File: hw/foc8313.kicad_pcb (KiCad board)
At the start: 4 copper layers, 35 x 35 mm, 83 parts, among them J1 Tag Connect, J2 CAN, J3 CAN, J4 Aux, P1 USB_C_Plug, SW1 SW_SPST, U1 DRV8313PWP, U10 XC6206P332MR, U2 STM32F103CBTx, U3 AS5047D, U4 INA240A2D, U5 INA240A2D, U6 ISO1050DUBR, U7 LMR36015SFBRNXR, U8 INA240A2D, U9 ZD24C08AE1-STGMT, X1 X322516MLB4SI

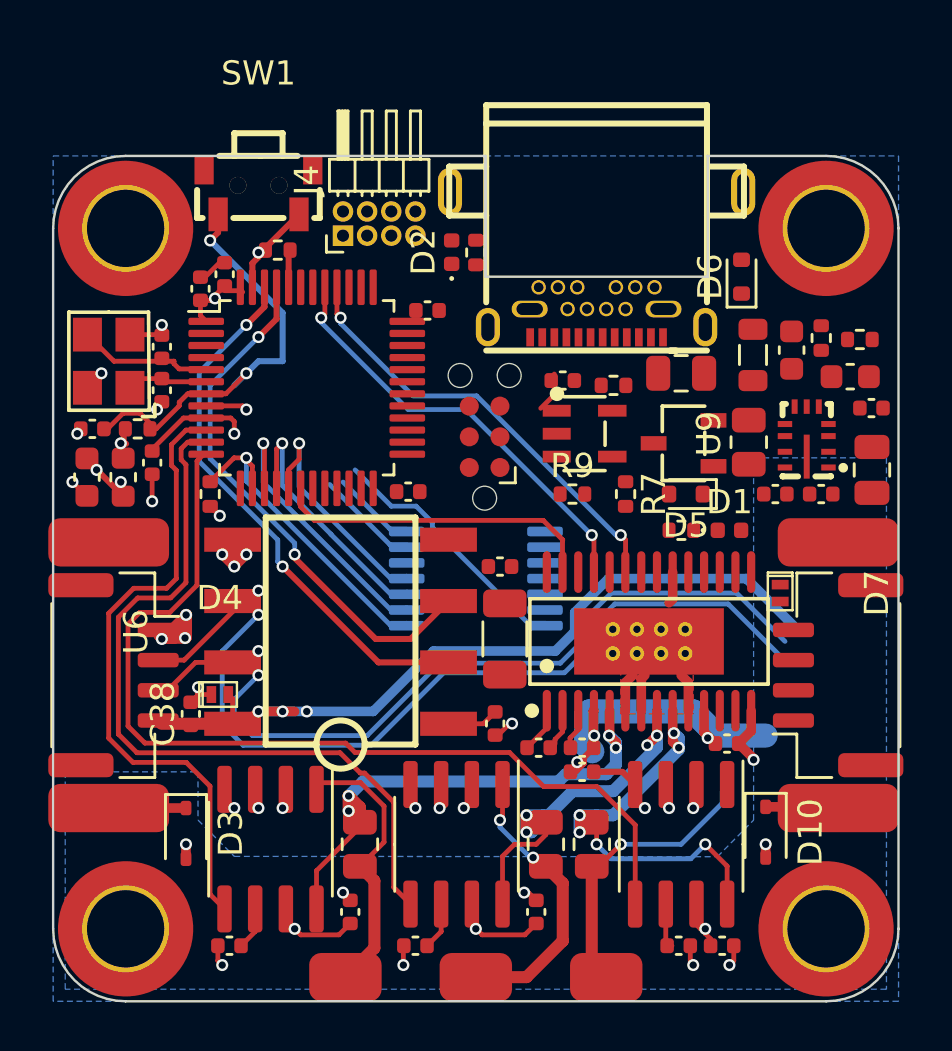
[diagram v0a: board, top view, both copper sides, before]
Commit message: [Hw] Cleaning up 5V section
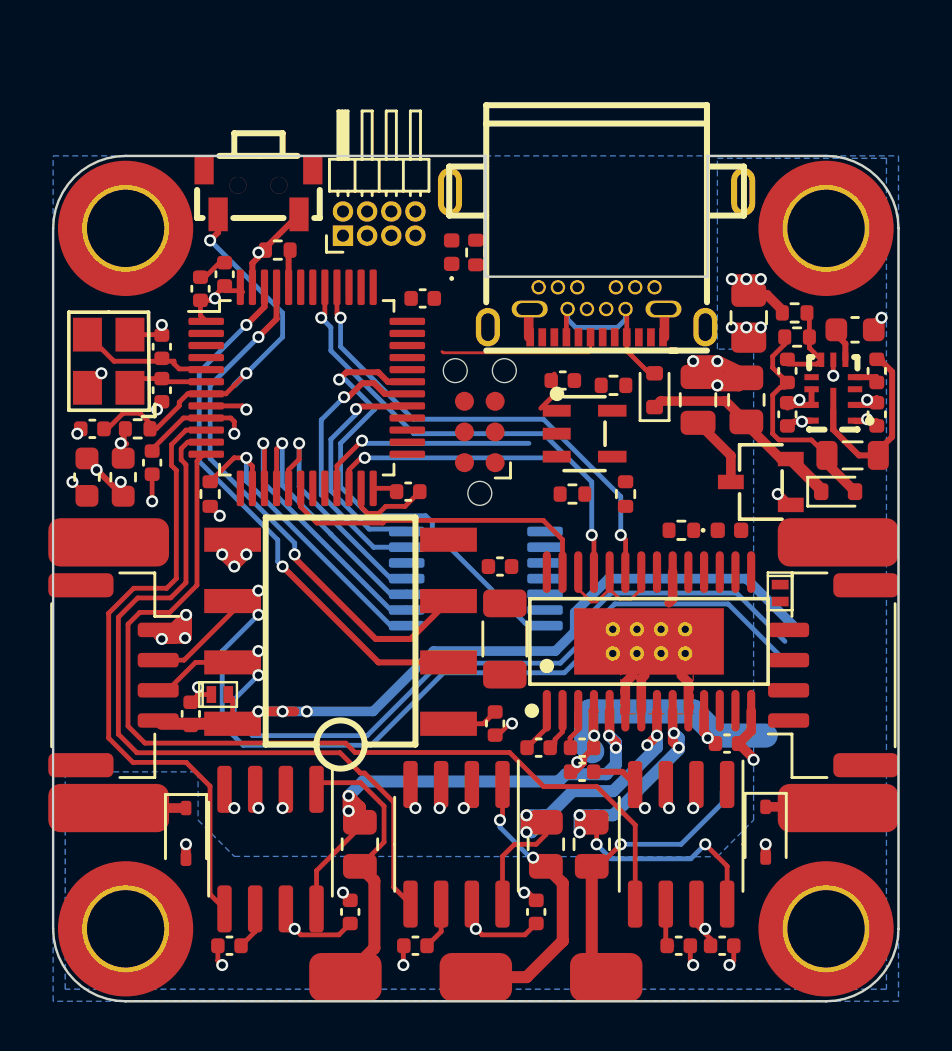
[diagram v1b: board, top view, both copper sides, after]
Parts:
- C18: footprint Capacitor_SMD:C_0603_1608Metric -> Capacitor_SMD:C_0402_1005Metric
- moved C16 8.11 mm to (151.3, 89.2), turned to 90 degrees
- moved D5 6.30 mm to (155.0, 96.4), turned to 0 degrees
- moved D6 5.92 mm to (147.4, 92.2)
- moved L3 5.86 mm to (155.6, 94.9), turned to 0 degrees
- moved C1 4.02 mm to (156.6, 93.2), turned to -90 degrees
- moved U10 3.58 mm to (151.8, 96.0)
- moved C2 3.34 mm to (152.9, 93.2), turned to -90 degrees
- moved R11 2.92 mm to (153.2, 89.0)
- moved U7 2.23 mm to (154.8, 92.2)
- moved C17 1.95 mm to (155.7, 89.7)
- moved C19 1.76 mm to (151.2, 92.6), turned to 90 degrees
- moved C21 1.56 mm to (156.6, 91.4), turned to -90 degrees
- moved C22 1.30 mm to (149.2, 92.6), turned to 90 degrees
- moved R10 1.00 mm to (153.3, 90.0), turned to 0 degrees
- moved C18 0.88 mm to (152.9, 91.4), turned to 90 degrees
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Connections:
- U2 pad 21: unconnected-(U2-PB10-Pad21) -> /I2C.SCL
- U2 pad 22: unconnected-(U2-PB11-Pad22) -> /I2C.SDA
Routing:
- net GND: track 38.7 -> 58.1 mm, vias 27 -> 38
- net Net-(D5-A): track 0.00 -> 9.48 mm
- net /ENC_Z: track 10.6 -> 20.0 mm, vias 0 -> 1
- net /I2C.SCL: track 0.00 -> 9.36 mm, vias 0 -> 1
- net /I2C.SDA: track 0.00 -> 9.02 mm, vias 0 -> 1
- net +5V: track 0.00 -> 8.67 mm
- net Net-(D6-A): track 0.00 -> 8.00 mm
- net Net-(U7-SW): track 0.00 -> 7.77 mm
- net /ENC_B: track 4.22 -> 11.9 mm, vias 0 -> 1
- net /USB_DM: track 0.00 -> 6.76 mm
- net /ENC_A: track 3.45 -> 9.79 mm, vias 0 -> 1
- net /DRV_EN: track 0.00 -> 5.50 mm
- net VCC: track 20.8 -> 25.8 mm, vias 3 -> 8
- net +3.3V: track 13.7 -> 17.7 mm
- net Net-(U7-FB): track 0.00 -> 3.62 mm
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
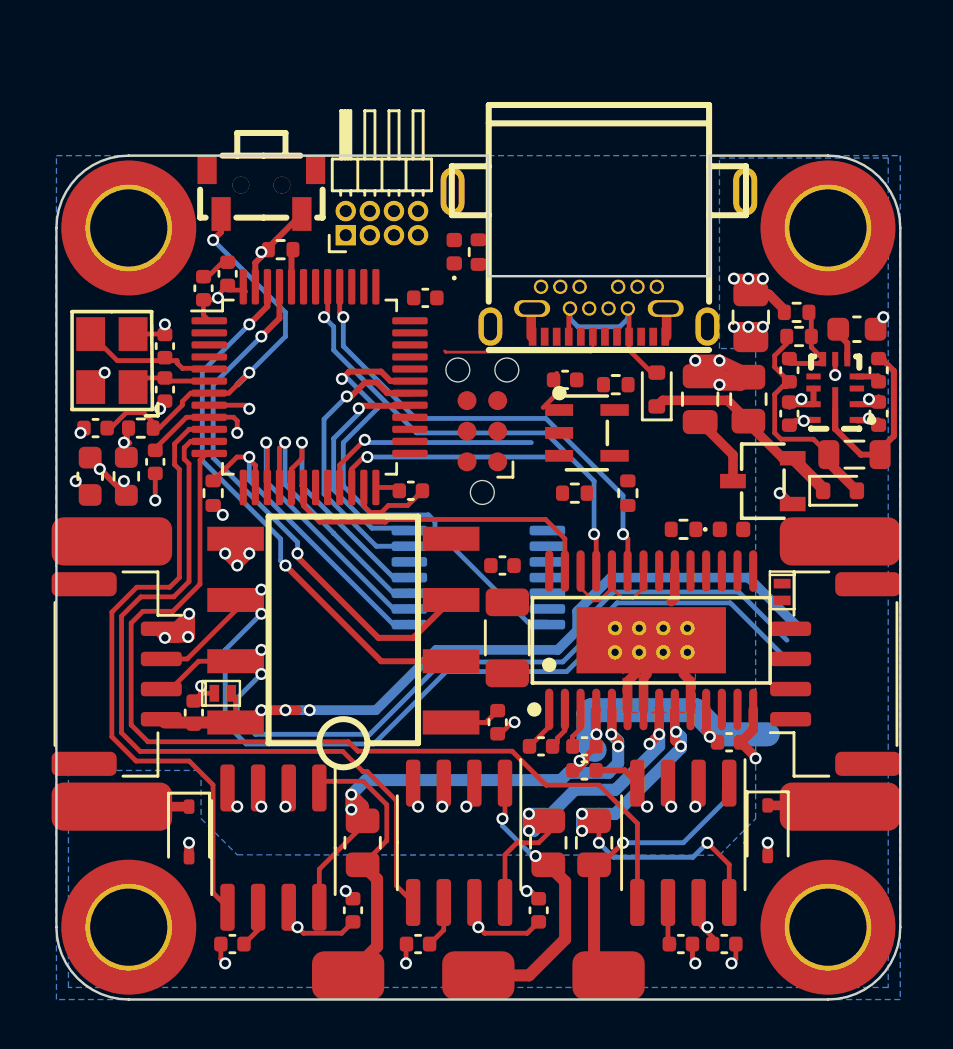
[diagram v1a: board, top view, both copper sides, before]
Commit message: [Hw] User button, tag connect placement, eeprom placement
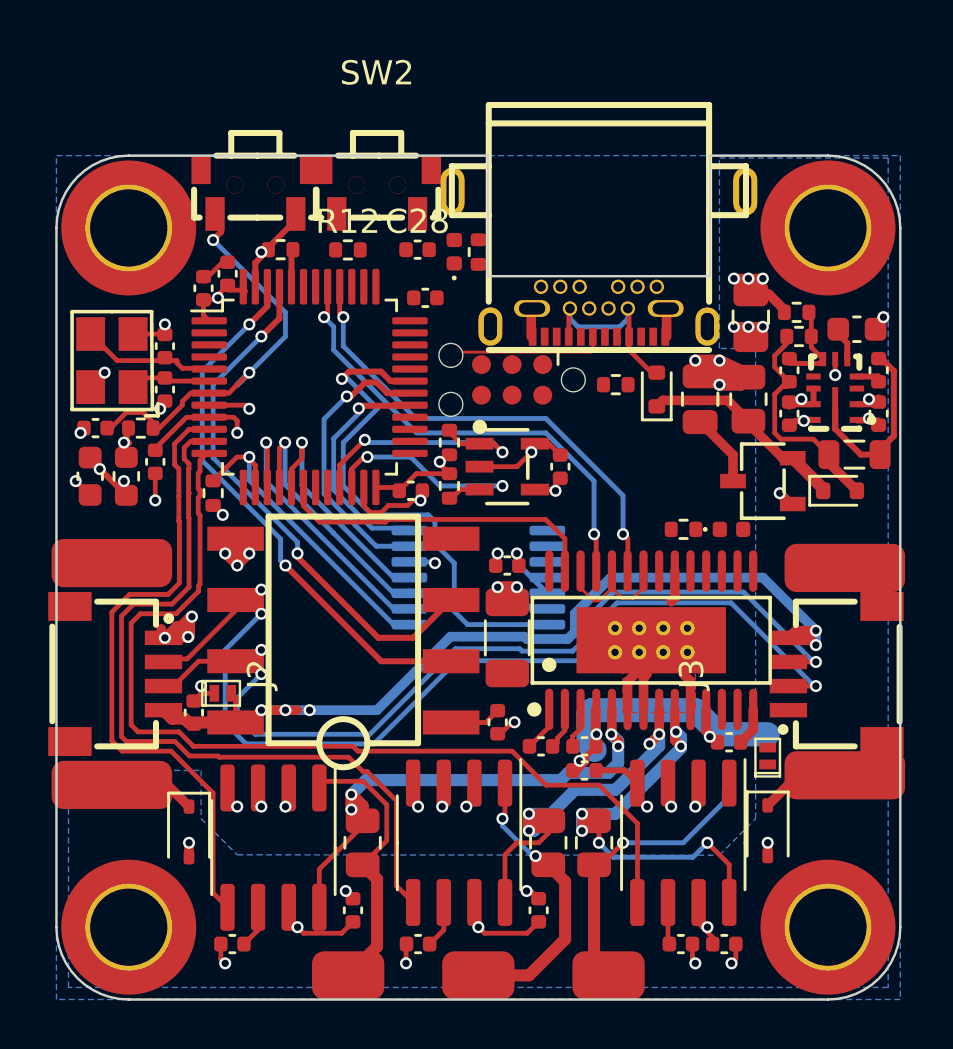
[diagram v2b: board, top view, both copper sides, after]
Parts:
- removed J4: Aux, Connector_PinHeader_1.00mm:PinHeader_2x04_P1.00mm_Horizontal
- added C28: 100n, Capacitor_SMD:C_0402_1005Metric, F.Cu at (137.5, 86.4)
- added R12: 100k, Resistor_SMD:R_0402_1005Metric, F.Cu at (134.6, 86.4)
- added SW2: SW_SPST, easyeda:SW-SMD_L4.7-W3.5-P3.35-EH, F.Cu at (135.8, 84.0)
- J2, J3: footprint Connector_JST:JST_GH_SM04B-GHS-TB_1x04-1MP_P1.25mm_Horizontal -> easyeda:CONN-SMD_4P-P1.00_INCP_IPCW100W14XXXXR
- moved R7 7.41 mm to (138.8, 96.2)
- moved D7 6.83 mm to (152.0, 107.4), turned to 90 degrees
- moved R9 5.61 mm to (138.8, 94.4), turned to 90 degrees
- moved C25 3.61 mm to (143.4, 95.4), turned to 90 degrees
- moved U9 3.58 mm to (141.2, 95.4)
- moved J1 2.46 mm to (141.4, 91.8), turned to 180 degrees
- moved H6 1.32 mm to (155.2, 108.2)
- moved H5 1.12 mm to (155.2, 99.6)
- moved H4 0.90 mm to (124.8, 108.6)
- moved H7 0.90 mm to (124.8, 99.4)
- moved SW1 0.25 mm to (130.8, 84.0)
- moved C7 0.20 mm to (141.2, 99.5)
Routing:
- net GND: track 58.1 -> 65.6 mm, vias 38 -> 43
- net +3V3: track 0.70 -> 5.85 mm, vias 1 -> 2
- net /CAN.V+: track 33.0 -> 37.1 mm, vias 3 -> 5
- net +3.3V: track 17.7 -> 21.1 mm, vias 2 -> 4
- net /CAN.L: track 38.0 -> 40.8 mm, vias 2 -> 3
- net /CAN.H: track 33.8 -> 36.5 mm, vias 2 -> 3
- net /ENC_Z: track 20.0 -> 21.6 mm
- net /I2C.SCL: track 9.36 -> 11.0 mm, vias 1 -> 2
- net VCC: track 25.8 -> 24.5 mm
- net /I2C.SDA: track 9.02 -> 9.12 mm, vias 1 -> 2

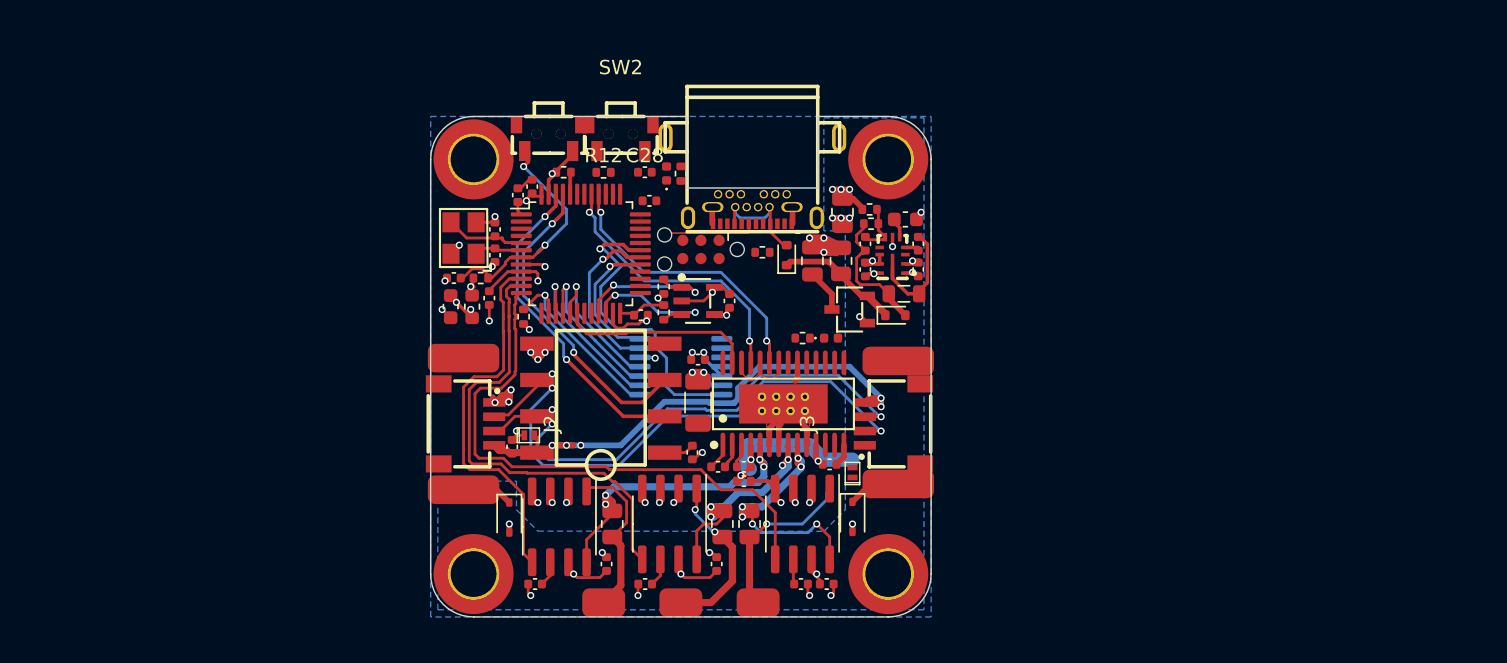
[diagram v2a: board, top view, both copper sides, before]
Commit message: [Hw] Small ICs to make 3 wire can possible in this formfactor
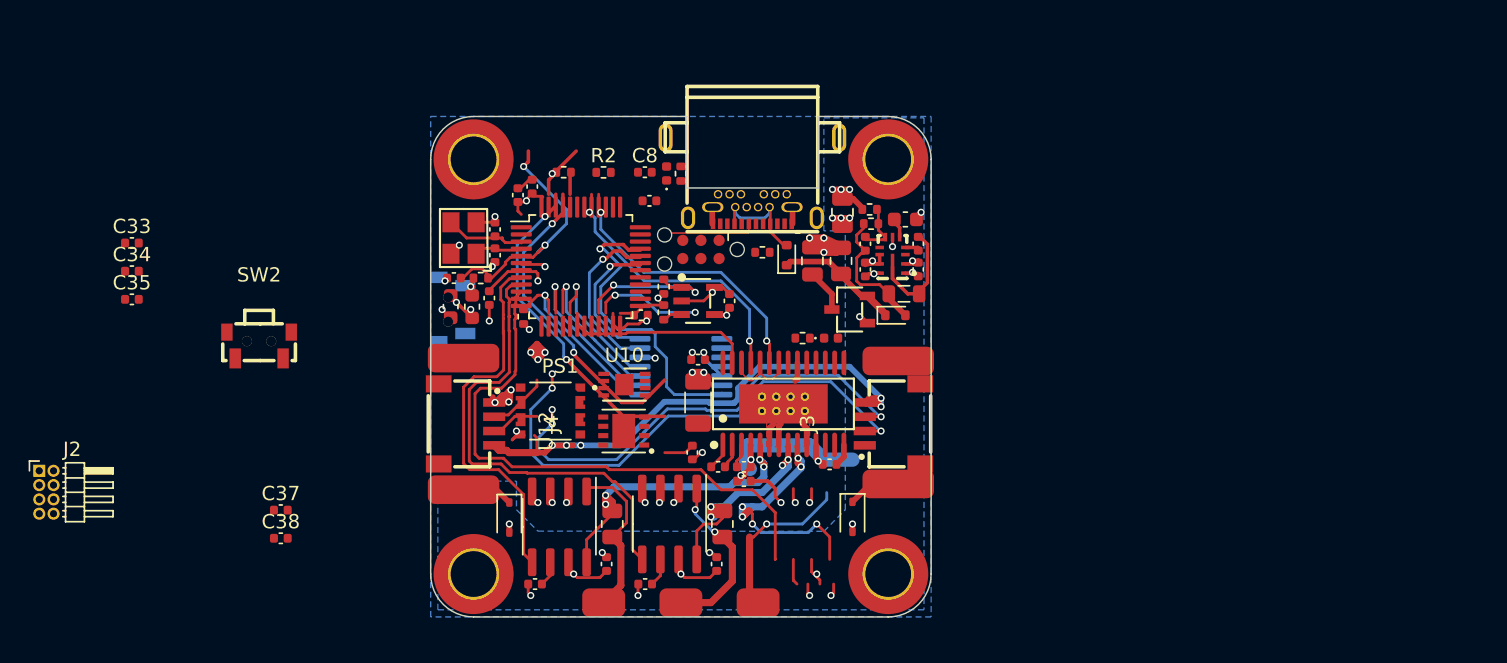
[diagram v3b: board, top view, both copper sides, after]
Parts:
- removed the C26 at (148.4, 115.2)
- removed the C27 at (150.2, 115.2)
- removed the D4 at (129.4, 104.8)
- removed D7: 5V, easyeda:X1-DFN1006-2_L1.0-W0.6-RD
- removed R15: 6m, Resistor_SMD:R_0805_2012Metric
- removed the U6 at (134.4, 102.2)
- removed the U8 at (148.5, 111.0)
- added C33: 100n, Capacitor_SMD:C_0402_1005Metric, F.Cu at (101.6, 91.3)
- added C34: 100n, Capacitor_SMD:C_0402_1005Metric, F.Cu at (101.6, 93.3)
- added C35: 100n, Capacitor_SMD:C_0402_1005Metric, F.Cu at (101.6, 95.3)
- added C37: 22uF, Capacitor_SMD:C_0402_1005Metric, F.Cu at (112.0, 110.0)
- added J2: Aux, Connector_PinHeader_1.00mm:PinHeader_2x04_P1.00mm_Horizontal, F.Cu at (95.1, 107.3)
- added PS1: MIE1W0505BGLVH-3R-Z, MIE1W0505BGLVH-3R-Z:CONV_MIE1W0505BGLVH-3R-Z, F.Cu at (130.9, 103.1)
- added U10: ~, Package_DFN_QFN:DFN-8-1EP_3x2mm_P0.5mm_EP1.3x1.5mm, F.Cu at (136.1, 101.2)
- added U12: TJA1051TK/3,118, easyeda:HVSON-8_L3.0-W3.0-P0.65-BL-EP, F.Cu at (136.0, 104.5)
- C38: value 100n -> 22uF
- SW1: moved to B.Cu
- moved SW2 29.2 mm to (110.5, 98.5)
- moved C38 17.4 mm to (112.0, 112.0), turned to 0 degrees
- moved SW1 13.8 mm to (124.0, 96.0), turned to -90 degrees
- moved U4 0.90 mm to (133.0, 93.0)
- renumbered C13 to C1, C1 to C10, C2 to C11, C21 to C12, C18 to C13, C19 to C14, C17 to C15, C15 to C16, C14 to C17, C22 to C18, C31 to C19, C12 to C2, C30 to C20, C29 to C21, C8 to C22, C3 to C23, C7 to C24, C20 to C26, C4 to C27, C23 to C28, C24 to C29, C11 to C3, C33 to C36, C10 to C4, C9 to C7, C28 to C8, C16 to C9, D10 to D1, D5 to D2, D1 to D4, D2 to D5, H4 to H1, H8 to H10, H9 to H11, H5 to H2, H6 to H3, H7 to H4, H1 to H5, H2 to H6, H10 to H7, H11 to H8, H3 to H9, J2 to J4, L2 to L1, L3 to L2, R9 to R10, R13 to R11, R4 to R12, R8 to R13, R12 to R2, R10 to R3, R11 to R4, R3 to R5, R2 to R6, R6 to R7, R5 to R8, R7 to R9, U7 to U1, U10 to U2, U1 to U3, U2 to U4, U3 to U5, U9 to U6, U4 to U7, U5 to U8
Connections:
- C38 pad 1: /CAN.V+ -> /isocan/ISO5V
- C38 pad 2: /CAN.V- -> /CAN.GND
- U3 pad 5: /PHC -> /OUTC
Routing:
- net /PHC: track 18.6 -> 0.00 mm, vias 6 -> 0
- net /PHA: track 20.7 -> 39.3 mm, vias 4 -> 9
- net /CAN.V-: track 12.3 -> 10.2 mm, vias 7 -> 6
- net /CAN.GND: track 0.00 -> 2.04 mm, vias 0 -> 1
- net /HSE_OUT: track 3.37 -> 5.09 mm, vias 0 -> 1
- net GND: track 65.6 -> 63.9 mm, vias 43 -> 42
- net /OUTC: vias 1 -> 2
